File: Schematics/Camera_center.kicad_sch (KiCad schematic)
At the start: 8 parts, among them J5 Runcam Split 4 v2, U6 TPS22917DBVR

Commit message: assigned footprints ready for pcb design
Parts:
- C28, C29, C30, C31, J5: footprint (none) -> Capacitor_SMD:C_0805_2012Metric_Pad1.18x1.45mm_HandSolder
- R10, R9: footprint (none) -> Resistor_SMD:R_0805_2012Metric_Pad1.20x1.40mm_HandSolder
- U6: footprint SOT95P280X145-6N -> myFootprints:SOT95P280X145-6N
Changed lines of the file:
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@@
 			)
 		)
-		(property "Footprint" ""
+		(property "Footprint" "Capacitor_SMD:C_0805_2012Metric_Pad1.18x1.45mm_HandSolder"
 			(at 65.7352 82.55 0)
 			(effects
@@
 			)
 		)
-		(property "Footprint" ""
+		(property "Footprint" "Capacitor_SMD:C_0805_2012Metric_Pad1.18x1.45mm_HandSolder"
 			(at 223.52 86.36 0)
 			(effects
@@
 			)
 		)
-		(property "Footprint" ""
+		(property "Footprint" "Capacitor_SMD:C_0805_2012Metric_Pad1.18x1.45mm_HandSolder"
 			(at 134.3152 90.17 0)
 			(effects
@@
 			)
 		)
-		(property "Footprint" ""
+		(property "Footprint" "Capacitor_SMD:C_0805_2012Metric_Pad1.18x1.45mm_HandSolder"
 			(at 147.0152 90.17 0)
 			(effects
@@
 			)
 		)
-		(property "Footprint" ""
+		(property "Footprint" "Capacitor_SMD:C_0805_2012Metric_Pad1.18x1.45mm_HandSolder"
 			(at 120.3452 90.17 0)
 			(effects
@@
 			)
 		)
-		(property "Footprint" "SOT95P280X145-6N"
+		(property "Footprint" "myFootprints:SOT95P280X145-6N"
 			(at 95.25 90.17 0)
 			(effects
@@
 			)
 		)
-		(property "Footprint" ""
+		(property "Footprint" "Resistor_SMD:R_0805_2012Metric_Pad1.20x1.40mm_HandSolder"
 			(at 197.612 78.74 90)
 			(effects
@@
 			)
 		)
-		(property "Footprint" ""
+		(property "Footprint" "Resistor_SMD:R_0805_2012Metric_Pad1.20x1.40mm_HandSolder"
 			(at 62.992 91.44 90)
 			(effects

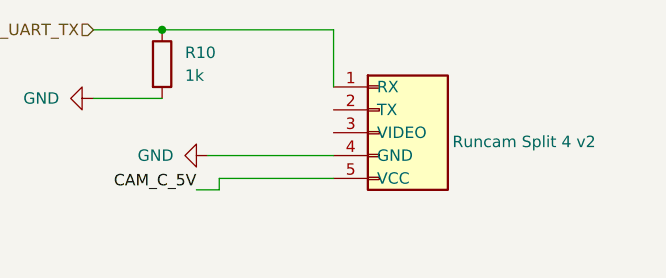
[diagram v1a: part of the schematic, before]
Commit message: Fixed Schematic and PCB refrences everything is connected correctly now
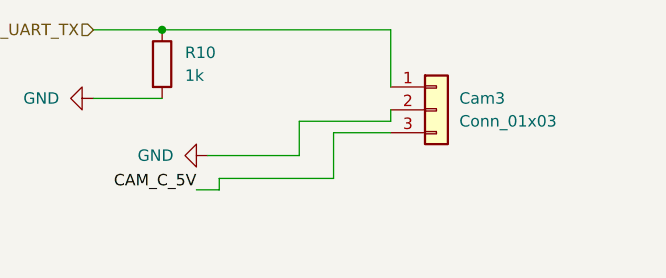
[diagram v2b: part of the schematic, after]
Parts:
- removed J5: Runcam Split 4 v2, Capacitor_SMD:C_0805_2012Metric_Pad1.18x1.45mm_HandSolder, symbol Connector_Generic:Conn_01x05
- added Cam3: Conn_01x03, Connector_JST:JST_PH_B3B-PH-K_1x03_P2.00mm_Vertical, symbol Connector_Generic:Conn_01x03
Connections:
- net CAM_UART_TX: now also Cam3.1 (Pin_1)
- net GND: now also Cam3.2 (Pin_2)
- net at C29.1, C30.1, C31.1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: now also Cam3.3 (Pin_3)
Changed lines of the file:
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@@
 	(wire
 		(pts
-			(xy 218.44 74.93) (xy 218.44 81.28)
+			(xy 224.79 74.93) (xy 224.79 81.28)
+		)
+		(stroke
+			(width 0)
+			(type default)
+		)
+	)
+	(wire
+		(pts
+			(xy 214.63 85.09) (xy 214.63 88.9)
 		)
 		(stroke
@@
 	(wire
 		(pts
+			(xy 218.44 91.44) (xy 218.44 86.36)
+		)
+		(stroke
+			(width 0)
+			(type default)
+		)
+	)
+	(wire
+		(pts
+			(xy 224.79 83.82) (xy 224.79 85.09)
+		)
+		(stroke
+			(width 0)
+			(type default)
+		)
+	)
+	(wire
+		(pts
 			(xy 110.49 97.79) (xy 118.11 97.79)
 		)
@@
 	(wire
 		(pts
+			(xy 218.44 86.36) (xy 224.79 86.36)
+		)
+		(stroke
+			(width 0)
+			(type default)
+		)
+	)
+	(wire
+		(pts
 			(xy 146.05 90.17) (xy 160.02 90.17)
 		)
@@
 	(wire
 		(pts
+			(xy 214.63 85.09) (xy 224.79 85.09)
+		)
+		(stroke
+			(width 0)
+			(type default)
+		)
+	)
+	(wire
+		(pts
 			(xy 119.38 82.55) (xy 133.35 82.55)
 		)
@@
 	(wire
 		(pts
-			(xy 204.47 88.9) (xy 218.44 88.9)
+			(xy 204.47 88.9) (xy 214.63 88.9)
 		)
 		(stroke
@@
 	(wire
 		(pts
-			(xy 199.39 74.93) (xy 218.44 74.93)
+			(xy 199.39 74.93) (xy 224.79 74.93)
 		)
 		(stroke
@@
 	)
 	(symbol
-		(lib_id "Connector_Generic:Conn_01x05")
-		(at 223.52 86.36 0)
-		(unit 1)
-		(exclude_from_sim no)
-		(in_bom yes)
-		(on_board yes)
-		(dnp no)
-		(fields_autoplaced yes)
-		(property "Reference" "J5"
-			(at 226.06 85.0899 0)
-			(effects
-				(font
-					(size 1.27 1.27)
-				)
-				(justify left)
-				(hide yes)
-			)
-		)
-		(property "Value" "Runcam Split 4 v2"
-			(at 231.648 87.376 0)
-			(effects
-				(font
-					(size 1.27 1.27)
-				)
-				(justify left)
-			)
-		)
-		(property "Footprint" "Capacitor_SMD:C_0805_2012Metric_Pad1.18x1.45mm_HandSolder"
-			(at 223.52 86.36 0)
-			(effects
-				(font
-					(size 1.27 1.27)
-				)
-				(hide yes)
-			)
-		)
-		(property "Datasheet" "~"
-			(at 223.52 86.36 0)
-			(effects
-				(font
-					(size 1.27 1.27)
-				)
-				(hide yes)
-			)
-		)
-		(property "Description" "Generic connector, single row, 01x05, script generated (kicad-library-utils/schlib/autogen/connector/)"
-			(at 222.504 75.438 0)
-			(effects
-				(font
-					(size 1.27 1.27)
-				)
-				(hide yes)
-			)
-		)
-		(pin "5"
-		)
-		(pin "4"
-		)
-		(pin "3"
-		)
-		(pin "1"
-		)
-		(pin "2"
-		)
-		(instances
-			(project "cameraBoardSchematic"
-				(path "/65068a32-f105-4204-b50e-234054c5a6d0/74e3c2e3-591c-4dbb-bedb-b7f7db2a7e7f"
-					(reference "J5")
-					(unit 1)
-				)
-			)
-		)
-	)
-	(symbol
 		(lib_id "Device:C")
 		(at 133.35 86.36 0)
@@
 					(unit 1)
 				)
+			)
+		)
+	)
+	(symbol
+		(lib_id "Connector_Generic:Conn_01x03")
+		(at 229.87 83.82 0)
+		(unit 1)
+		(exclude_from_sim no)
+		(in_bom yes)
+		(on_board yes)
+		(dnp no)
+		(fields_autoplaced yes)
+		(property "Reference" "Cam3"
+			(at 232.41 82.5499 0)
+			(effects
+				(font
+					(size 1.27 1.27)
+				)
+				(justify left)
+			)
+		)
+		(property "Value" "Conn_01x03"
+			(at 232.41 85.0899 0)
+			(effects
+				(font
+					(size 1.27 1.27)
+				)
+				(justify left)
+			)
+		)
+		(property "Footprint" "Connector_JST:JST_PH_B3B-PH-K_1x03_P2.00mm_Vertical"
+			(at 229.87 83.82 0)
+			(effects
+				(font
+					(size 1.27 1.27)
+				)
+				(hide yes)
+			)
+		)
+		(property "Datasheet" "~"
+			(at 229.87 83.82 0)
+			(effects
+				(font
+					(size 1.27 1.27)
+				)
+				(hide yes)
+			)
+		)
+		(property "Description" "Generic connector, single row, 01x03, script generated (kicad-library-utils/schlib/autogen/connector/)"
+			(at 229.87 83.82 0)
+			(effects
+				(font
+					(size 1.27 1.27)
+				)
+				(hide yes)
+			)
+		)
+		(pin "1"
+		)
+		(pin "2"
+		)
+		(pin "3"
+		)
+		(instances
+			(project "CameraBoard"
+				(path "/65068a32-f105-4204-b50e-234054c5a6d0/74e3c2e3-591c-4dbb-bedb-b7f7db2a7e7f"
+					(reference "Cam3")
+					(unit 1)
+				)

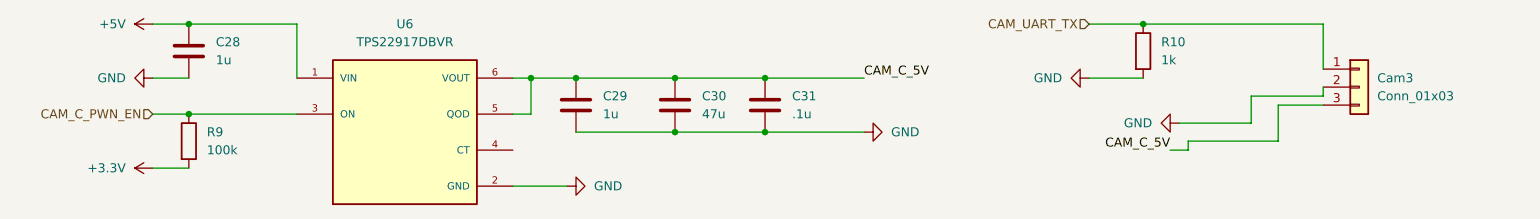
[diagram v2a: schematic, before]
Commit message: routing taking place only USB to do
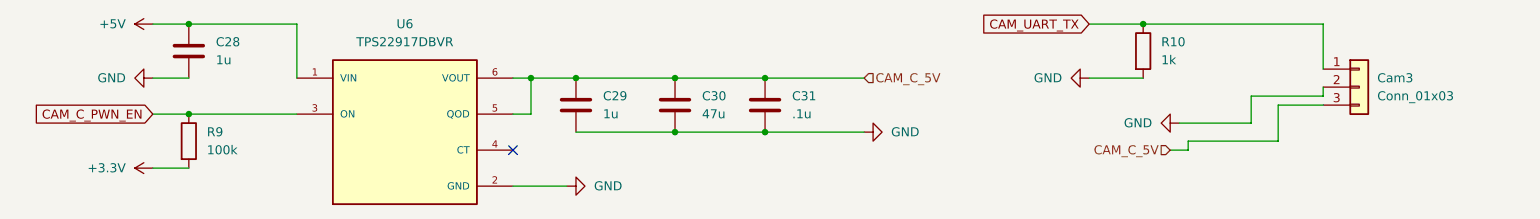
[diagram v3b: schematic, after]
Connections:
- net CAM_C_5V: now reaches C29.1, C30.1, C31.1, Cam3.3 (Pin_3), U6.5 (QOD), U6.6 (VOUT)
- no-connect marks 0 -> 1
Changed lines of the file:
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@@
 		(color 0 0 0 0)
+	)
+	(no_connect
+		(at 110.49 92.71)
 	)
 	(wire
@@
 		)
 	)
-	(label "CAM_C_5V"
-		(at 203.2 92.71 180)
-		(effects
-			(font
-				(size 1.27 1.27)
-			)
-			(justify right bottom)
-		)
-	)
-	(label "CAM_C_5V"
-		(at 160.02 82.55 0)
-		(effects
-			(font
-				(size 1.27 1.27)
-			)
-			(justify left bottom)
-		)
-	)
-	(hierarchical_label "CAM_C_PWN_EN"
+	(global_label "CAM_C_PWN_EN"
 		(shape input)
 		(at 59.69 87.63 180)
+		(fields_autoplaced yes)
 		(effects
 			(font
@@
 			(justify right)
 		)
-	)
-	(hierarchical_label "CAM_UART_TX"
+		(property "Intersheetrefs" "${INTERSHEET_REFS}"
+			(at 42.1906 87.63 0)
+			(effects
+				(font
+					(size 1.27 1.27)
+				)
+				(justify right)
+				(hide yes)
+			)
+		)
+	)
+	(global_label "CAM_UART_TX"
 		(shape input)
 		(at 191.77 74.93 180)
+		(fields_autoplaced yes)
 		(effects
 			(font
@@
 			(justify right)
 		)
-	)
+		(property "Intersheetrefs" "${INTERSHEET_REFS}"
+			(at 176.2058 74.93 0)
+			(effects
+				(font
+					(size 1.27 1.27)
+				)
+				(justify right)
+				(hide yes)
+			)
+		)
+	)
+	(hierarchical_label "CAM_C_5V"
+		(shape input)
+		(at 203.2 92.71 180)
+		(effects
+			(font
+				(size 1.27 1.27)
+			)
+			(justify right)
+		)
+	)
+	(hierarchical_label "CAM_C_5V"
+		(shape input)
+		(at 160.02 82.55 0)
+		(effects
+			(font
+				(size 1.27 1.27)
+			)
+			(justify left)
+		)
+	)

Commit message: Cleaned up schematic added ocilator added jtag 10 pin begining routing again
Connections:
- net CAM_C_5V: no longer names the net of C29.1, C30.1, C31.1, Cam3.3 (Pin_3), U6.5 (QOD), U6.6 (VOUT)
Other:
- moved on the sheet: Cam3, R10
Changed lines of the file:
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@@
+	)
+	(junction
+		(at 199.39 88.9)
+		(diameter 0)
+		(color 0 0 0 0)
 	)
 	(junction
@@
 	)
 	(junction
-		(at 199.39 74.93)
+		(at 199.39 81.28)
 		(diameter 0)
 		(color 0 0 0 0)
@@
 	(wire
 		(pts
-			(xy 205.74 92.71) (xy 205.74 91.44)
-		)
-		(stroke
-			(width 0)
-			(type default)
-		)
-	)
-	(wire
-		(pts
-			(xy 224.79 74.93) (xy 224.79 81.28)
-		)
-		(stroke
-			(width 0)
-			(type default)
-		)
-	)
-	(wire
-		(pts
-			(xy 214.63 85.09) (xy 214.63 88.9)
+			(xy 186.69 92.71) (xy 186.69 91.44)
+		)
+		(stroke
+			(width 0)
+			(type default)
+		)
+	)
+	(wire
+		(pts
+			(xy 224.79 81.28) (xy 224.79 85.09)
 		)
 		(stroke
@@
 	(wire
 		(pts
-			(xy 218.44 91.44) (xy 218.44 86.36)
-		)
-		(stroke
-			(width 0)
-			(type default)
-		)
-	)
-	(wire
-		(pts
-			(xy 224.79 83.82) (xy 224.79 85.09)
+			(xy 218.44 91.44) (xy 218.44 90.17)
+		)
+		(stroke
+			(width 0)
+			(type default)
+		)
+	)
+	(wire
+		(pts
+			(xy 224.79 87.63) (xy 224.79 88.9)
+		)
+		(stroke
+			(width 0)
+			(type default)
+		)
+	)
+	(wire
+		(pts
+			(xy 199.39 88.9) (xy 224.79 88.9)
 		)
 		(stroke
@@
 	(wire
 		(pts
-			(xy 203.2 92.71) (xy 205.74 92.71)
-		)
-		(stroke
-			(width 0)
-			(type default)
-		)
-	)
-	(wire
-		(pts
-			(xy 191.77 82.55) (xy 199.39 82.55)
+			(xy 184.15 92.71) (xy 186.69 92.71)
 		)
 		(stroke
@@
 	(wire
 		(pts
-			(xy 218.44 86.36) (xy 224.79 86.36)
+			(xy 218.44 90.17) (xy 224.79 90.17)
 		)
 		(stroke
@@
 	(wire
 		(pts
-			(xy 205.74 91.44) (xy 218.44 91.44)
-		)
-		(stroke
-			(width 0)
-			(type default)
-		)
-	)
-	(wire
-		(pts
-			(xy 214.63 85.09) (xy 224.79 85.09)
+			(xy 186.69 91.44) (xy 218.44 91.44)
 		)
 		(stroke
@@
 	(wire
 		(pts
-			(xy 204.47 88.9) (xy 214.63 88.9)
+			(xy 185.42 88.9) (xy 199.39 88.9)
 		)
 		(stroke
@@
 	(wire
 		(pts
-			(xy 199.39 74.93) (xy 224.79 74.93)
-		)
-		(stroke
-			(width 0)
-			(type default)
-		)
-	)
-	(wire
-		(pts
-			(xy 191.77 74.93) (xy 199.39 74.93)
+			(xy 199.39 81.28) (xy 224.79 81.28)
+		)
+		(stroke
+			(width 0)
+			(type default)
+		)
+	)
+	(wire
+		(pts
+			(xy 191.77 81.28) (xy 199.39 81.28)
 		)
 		(stroke
@@
 		)
 	)
-	(global_label "CAM_C_PWN_EN"
-		(shape input)
-		(at 59.69 87.63 180)
-		(fields_autoplaced yes)
-		(effects
-			(font
-				(size 1.27 1.27)
-			)
-			(justify right)
-		)
-		(property "Intersheetrefs" "${INTERSHEET_REFS}"
-			(at 42.1906 87.63 0)
-			(effects
-				(font
-					(size 1.27 1.27)
-				)
-				(justify right)
-				(hide yes)
-			)
-		)
-	)
-	(global_label "CAM_UART_TX"
-		(shape input)
-		(at 191.77 74.93 180)
-		(fields_autoplaced yes)
-		(effects
-			(font
-				(size 1.27 1.27)
-			)
-			(justify right)
-		)
-		(property "Intersheetrefs" "${INTERSHEET_REFS}"
-			(at 176.2058 74.93 0)
-			(effects
-				(font
-					(size 1.27 1.27)
-				)
-				(justify right)
-				(hide yes)
-			)
-		)
-	)
-	(hierarchical_label "CAM_C_5V"
-		(shape input)
-		(at 203.2 92.71 180)
-		(effects
-			(font
-				(size 1.27 1.27)
-			)
-			(justify right)
-		)
-	)
-	(hierarchical_label "CAM_C_5V"
-		(shape input)
+	(label "CAM_C_5V"
 		(at 160.02 82.55 0)
 		(effects
@@
 				(size 1.27 1.27)
 			)
-			(justify left)
+			(justify left bottom)
+		)
+	)
+	(label "CAM_C_5V"
+		(at 184.15 92.71 180)
+		(effects
+			(font
+				(size 1.27 1.27)
+			)
+			(justify right bottom)
+		)
+	)
+	(hierarchical_label "CAM_UART_TX"
+		(shape input)
+		(at 191.77 81.28 180)
+		(effects
+			(font
+				(size 1.27 1.27)
+			)
+			(justify right)
+		)
+	)
+	(hierarchical_label "CAM_C_PWN_EN"
+		(shape input)
+		(at 59.69 87.63 180)
+		(effects
+			(font
+				(size 1.27 1.27)
+			)
+			(justify right)
 		)
 	)
@@
 	(symbol
 		(lib_id "power:GND")
-		(at 204.47 88.9 270)
+		(at 185.42 88.9 270)
 		(unit 1)
 		(exclude_from_sim no)
@@
 		(fields_autoplaced yes)
 		(property "Reference" "#PWR040"
-			(at 198.12 88.9 0)
+			(at 179.07 88.9 0)
 			(effects
 				(font
@@
 		)
 		(property "Value" "GND"
-			(at 200.66 88.8999 90)
+			(at 181.61 88.8999 90)
 			(effects
 				(font
@@
 		)
 		(property "Footprint" ""
-			(at 204.47 88.9 0)
+			(at 185.42 88.9 0)
 			(effects
 				(font
@@
 		)
 		(property "Datasheet" ""
-			(at 204.47 88.9 0)
+			(at 185.42 88.9 0)
 			(effects
 				(font
@@
 		)
 		(property "Description" "Power symbol creates a global label with name \"GND\" , ground"
-			(at 204.47 88.9 0)
+			(at 185.42 88.9 0)
 			(effects
 				(font
@@
 				(path "/65068a32-f105-4204-b50e-234054c5a6d0/74e3c2e3-591c-4dbb-bedb-b7f7db2a7e7f"
 					(reference "#PWR040")
-					(unit 1)
-				)
-			)
-		)
-	)
-	(symbol
-		(lib_id "power:GND")
-		(at 191.77 82.55 270)
-		(unit 1)
-		(exclude_from_sim no)
-		(in_bom yes)
-		(on_board yes)
-		(dnp no)
-		(fields_autoplaced yes)
-		(property "Reference" "#PWR039"
-			(at 185.42 82.55 0)
-			(effects
-				(font
-					(size 1.27 1.27)
-				)
-				(hide yes)
-			)
-		)
-		(property "Value" "GND"
-			(at 187.96 82.5499 90)
-			(effects
-				(font
-					(size 1.27 1.27)
-				)
-				(justify right)
-			)
-		)
-		(property "Footprint" ""
-			(at 191.77 82.55 0)
-			(effects
-				(font
-					(size 1.27 1.27)
-				)
-				(hide yes)
-			)
-		)
-		(property "Datasheet" ""
-			(at 191.77 82.55 0)
-			(effects
-				(font
-					(size 1.27 1.27)
-				)
-				(hide yes)
-			)
-		)
-		(property "Description" "Power symbol creates a global label with name \"GND\" , ground"
-			(at 191.77 82.55 0)
-			(effects
-				(font
-					(size 1.27 1.27)
-				)
-				(hide yes)
-			)
-		)
-		(pin "1"
-		)
-		(instances
-			(project "cameraBoardSchematic"
-				(path "/65068a32-f105-4204-b50e-234054c5a6d0/74e3c2e3-591c-4dbb-bedb-b7f7db2a7e7f"
-					(reference "#PWR039")
 					(unit 1)
 				)
@@
 	(symbol
 		(lib_id "Device:R")
-		(at 199.39 78.74 0)
+		(at 199.39 85.09 0)
 		(unit 1)
 		(exclude_from_sim no)
@@
 		(fields_autoplaced yes)
 		(property "Reference" "R10"
-			(at 201.93 77.4699 0)
+			(at 201.93 83.8199 0)
 			(effects
 				(font
@@
 		)
 		(property "Value" "1k"
-			(at 201.93 80.0099 0)
+			(at 201.93 86.3599 0)
 			(effects
 				(font
@@
 		)
 		(property "Footprint" "Resistor_SMD:R_0805_2012Metric_Pad1.20x1.40mm_HandSolder"
-			(at 197.612 78.74 90)
+			(at 197.612 85.09 90)
 			(effects
 				(font
@@
 		)
 		(property "Datasheet" "~"
-			(at 199.39 78.74 0)
+			(at 199.39 85.09 0)
 			(effects
 				(font
@@
 		)
 		(property "Description" "Resistor"
-			(at 199.39 78.74 0)
+			(at 199.39 85.09 0)
 			(effects
 				(font
@@
 	(symbol
 		(lib_id "Connector_Generic:Conn_01x03")
-		(at 229.87 83.82 0)
+		(at 229.87 87.63 0)
 		(unit 1)
 		(exclude_from_sim no)
@@
 		(fields_autoplaced yes)
 		(property "Reference" "Cam3"
-			(at 232.41 82.5499 0)
+			(at 232.41 86.3599 0)
 			(effects
 				(font
@@
 		)
 		(property "Value" "Conn_01x03"
-			(at 232.41 85.0899 0)
+			(at 232.41 88.8999 0)
 			(effects
 				(font
@@
 		)
 		(property "Footprint" "Connector_JST:JST_PH_B3B-PH-K_1x03_P2.00mm_Vertical"
-			(at 229.87 83.82 0)
+			(at 229.87 87.63 0)
 			(effects
 				(font
@@
 		)
 		(property "Datasheet" "~"
-			(at 229.87 83.82 0)
+			(at 229.87 87.63 0)
 			(effects
 				(font
@@
 		)
 		(property "Description" "Generic connector, single row, 01x03, script generated (kicad-library-utils/schlib/autogen/connector/)"
-			(at 229.87 83.82 0)
-			(effects
-				(font
+			(at 229.87 87.63 0)
+			(effects
+				(font

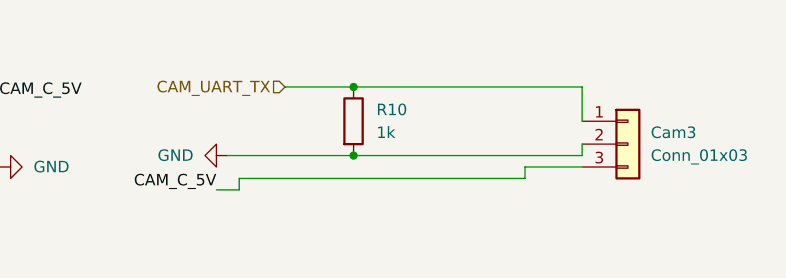
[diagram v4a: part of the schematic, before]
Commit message: second final draft finished routing added swd debug with stlink capabilities pending review for and data sheet review to ensure parts are correct, also need to edge cut ocillator
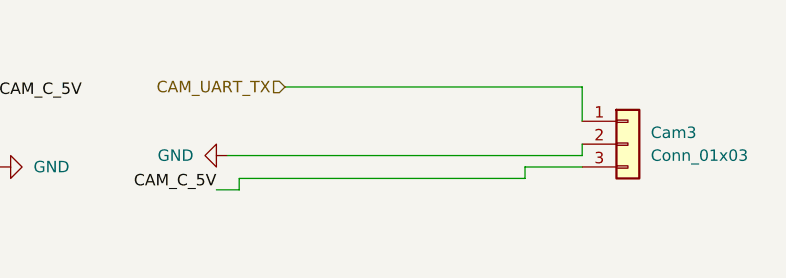
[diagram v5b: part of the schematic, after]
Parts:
- removed R10: 1k, Resistor_SMD:R_0805_2012Metric_Pad1.20x1.40mm_HandSolder, symbol Device:R
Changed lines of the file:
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@@
-	)
-	(junction
-		(at 199.39 88.9)
-		(diameter 0)
-		(color 0 0 0 0)
 	)
 	(junction
@@
 		(color 0 0 0 0)
 	)
-	(junction
-		(at 199.39 81.28)
-		(diameter 0)
-		(color 0 0 0 0)
-	)
 	(no_connect
 		(at 110.49 92.71)
@@
 	(wire
 		(pts
-			(xy 199.39 88.9) (xy 224.79 88.9)
+			(xy 185.42 88.9) (xy 224.79 88.9)
 		)
 		(stroke
@@
 	(wire
 		(pts
-			(xy 185.42 88.9) (xy 199.39 88.9)
-		)
-		(stroke
-			(width 0)
-			(type default)
-		)
-	)
-	(wire
-		(pts
 			(xy 110.49 82.55) (xy 113.03 82.55)
 		)
@@
 	(wire
 		(pts
-			(xy 199.39 81.28) (xy 224.79 81.28)
-		)
-		(stroke
-			(width 0)
-			(type default)
-		)
-	)
-	(wire
-		(pts
-			(xy 191.77 81.28) (xy 199.39 81.28)
+			(xy 191.77 81.28) (xy 224.79 81.28)
 		)
 		(stroke
@@
 					(unit 1)
 				)
-			)
-		)
-	)
-	(symbol
-		(lib_id "Device:R")
-		(at 199.39 85.09 0)
-		(unit 1)
-		(exclude_from_sim no)
-		(in_bom yes)
-		(on_board yes)
-		(dnp no)
-		(fields_autoplaced yes)
-		(property "Reference" "R10"
-			(at 201.93 83.8199 0)
-			(effects
-				(font
-					(size 1.27 1.27)
-				)
-				(justify left)
-			)
-		)
-		(property "Value" "1k"
-			(at 201.93 86.3599 0)
-			(effects
-				(font
-					(size 1.27 1.27)
-				)
-				(justify left)
-			)
-		)
-		(property "Footprint" "Resistor_SMD:R_0805_2012Metric_Pad1.20x1.40mm_HandSolder"
-			(at 197.612 85.09 90)
-			(effects
-				(font
-					(size 1.27 1.27)
-				)
-				(hide yes)
-			)
-		)
-		(property "Datasheet" "~"
-			(at 199.39 85.09 0)
-			(effects
-				(font
-					(size 1.27 1.27)
-				)
-				(hide yes)
-			)
-		)
-		(property "Description" "Resistor"
-			(at 199.39 85.09 0)
-			(effects
-				(font
-					(size 1.27 1.27)
-				)
-				(hide yes)
-			)
-		)
-		(pin "2"
-		)
-		(pin "1"
-		)
-		(instances
-			(project "cameraBoardSchematic"
-				(path "/65068a32-f105-4204-b50e-234054c5a6d0/74e3c2e3-591c-4dbb-bedb-b7f7db2a7e7f"
-					(reference "R10")
-					(unit 1)
-				)
